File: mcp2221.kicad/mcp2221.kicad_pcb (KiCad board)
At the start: 2 copper layers, 47.2 x 32.8 mm, 26 parts, among them J1 Jumper 32 or 21, J2 Conn_01x04_Male, J3 Conn_01x03_Male, J4 Conn_01x06_Male, J5 Conn_01x03_Male, J6 Conn_01x06_Male, J7 Conn_01x02_Male, J8 Conn_01x02_Male, SW1 SW_Push, SW2 SW_Push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

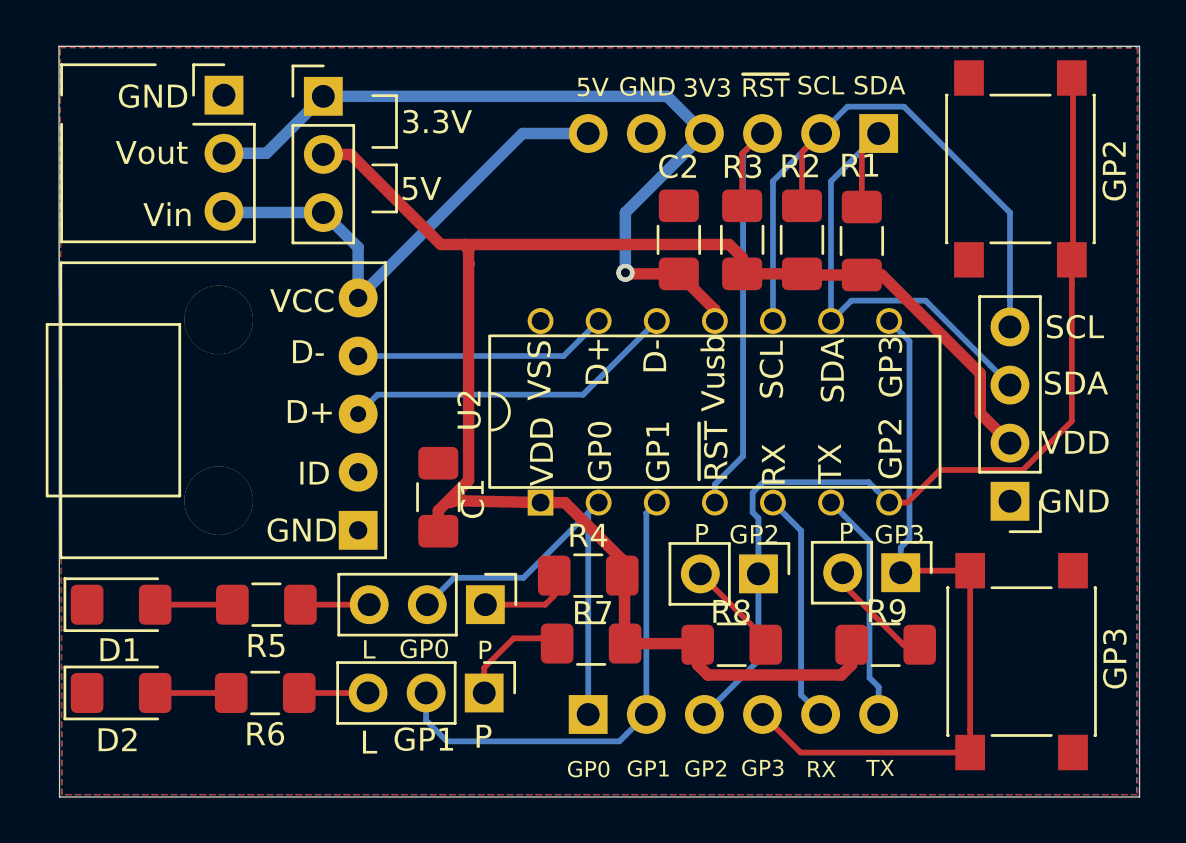
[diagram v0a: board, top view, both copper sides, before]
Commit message: changed to larger pads on SMD-footprints
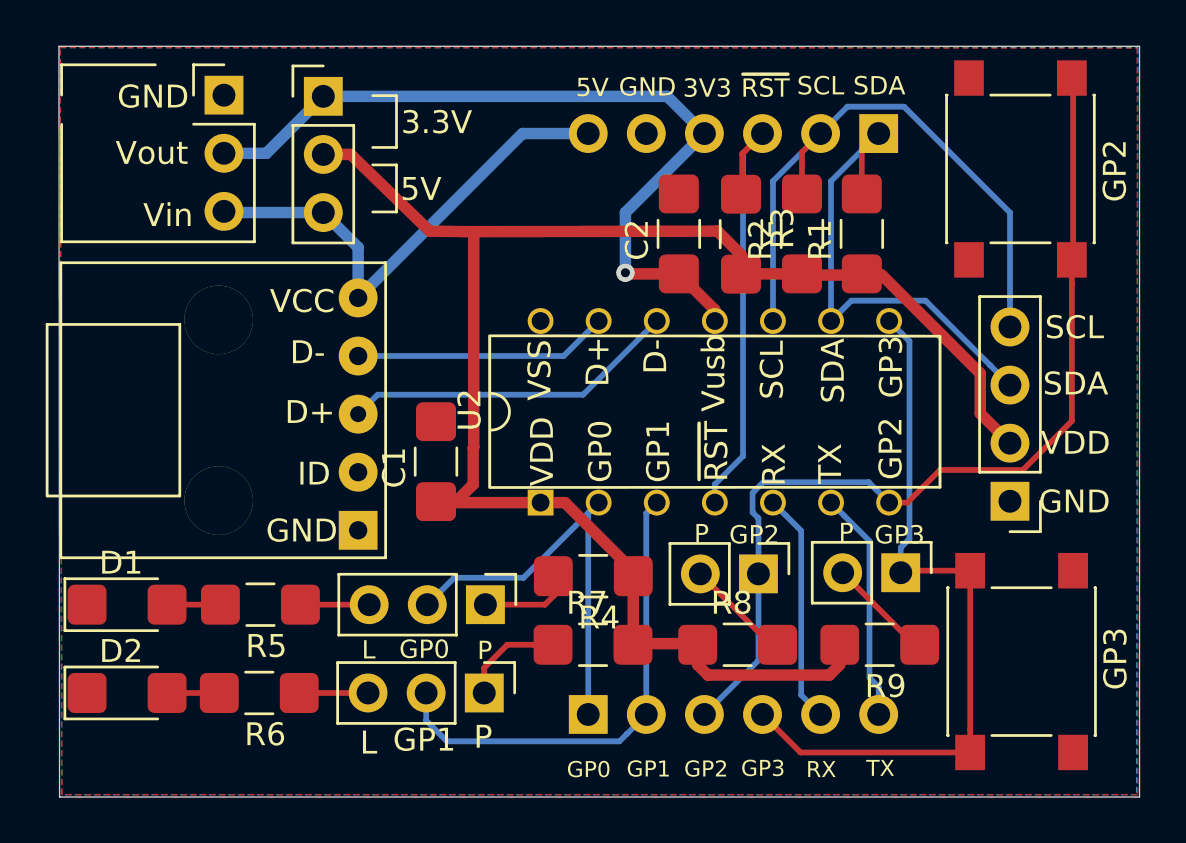
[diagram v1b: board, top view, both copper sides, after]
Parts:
- C1, C2: footprint Capacitor_SMD:C_1206_3216Metric_Pad1.42x1.75mm_HandSolder -> user:C_1206_3216_Pad1.7x1.75mm_BB
- D1, D2: footprint LED_SMD:LED_1206_3216Metric_Pad1.42x1.75mm_HandSolder -> user:LED_1206_3216_Pad1.7x1.75mm_BB
- R1, R2, R3, R4, R5, R6, R7, R8, R9: footprint Resistor_SMD:R_1206_3216Metric_Pad1.42x1.75mm_HandSolder -> user:R_1206_3216_Pad1.7x1.75mm_BB
- moved C1 1.30 mm to (80.8, 67.3)
- moved R3 0.51 mm to (94.1, 56.8)
- moved R4 0.48 mm to (87.9, 72.0)
- moved R7 0.18 mm to (87.4, 75.0)
- moved R1 0.05 mm to (99.4, 57.3)
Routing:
- net Net-(J3-Pad1): track 4.05 -> 4.87 mm

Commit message: changed I2C-connector
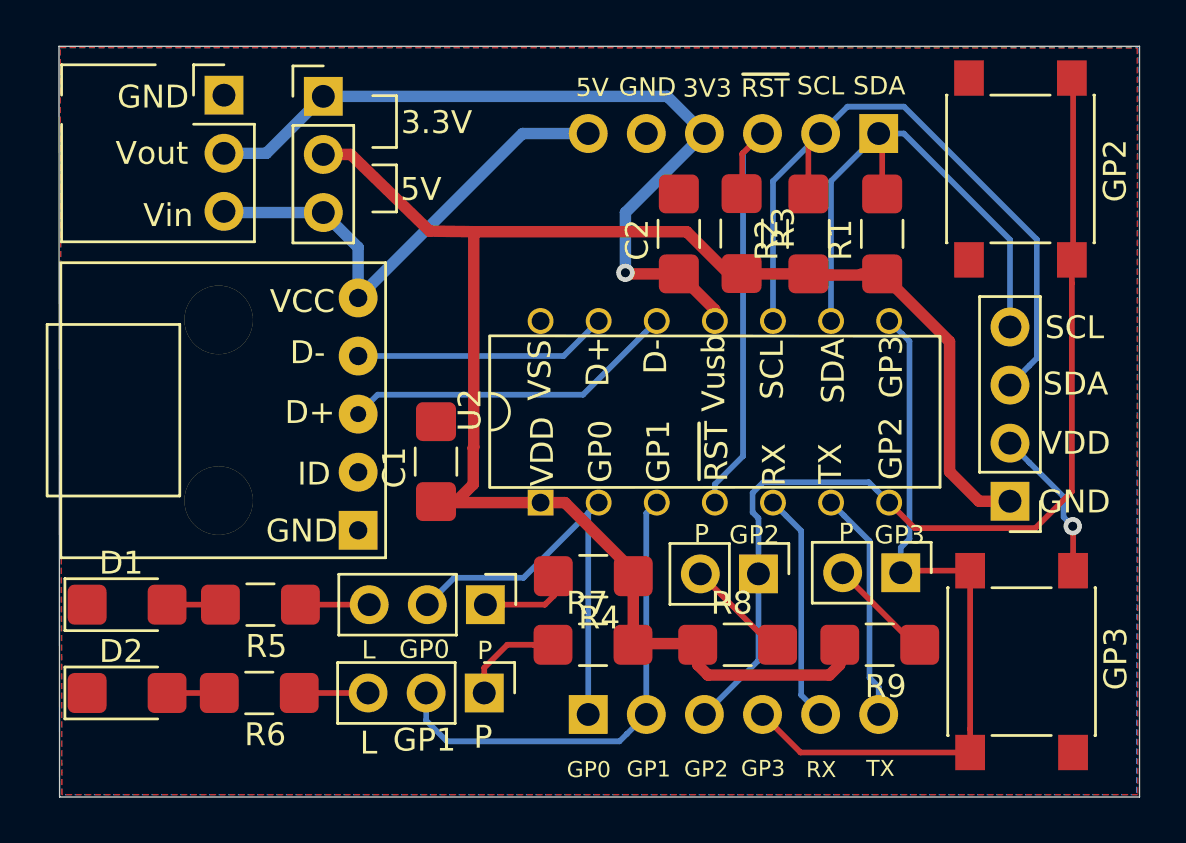
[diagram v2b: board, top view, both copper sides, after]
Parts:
- moved R1 3.51 mm to (100.3, 57.3)
- moved R2 2.34 mm to (97.1, 57.3)
- renumbered R2 to R1, R1 to R2
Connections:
- J2 pad 1: GND -> /VDD
- J2 pad 2: /VDD -> GND
- J2 pad 3: /SDA -> /SCL
- J2 pad 4: /SCL -> /SDA
- R1 pad 2: /SCL -> /SDA
- R2 pad 2: /SDA -> /SCL
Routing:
- net GND: track 0.00 -> 6.72 mm, vias 0 -> 1
- net /VDD: track 74.9 -> 77.8 mm
- net /SCL: track 28.2 -> 31.1 mm
- net /GP2: track 41.8 -> 44.5 mm
- net /SDA: track 22.3 -> 24.3 mm

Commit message: changed revision-number to 8
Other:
- board text added: "Rev 8"
- board text removed: "Rev 7"
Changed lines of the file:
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@@
     (effects (font (size 0.8 0.8) (thickness 0.15)))
   )
-  (gr_text "Rev 7" (at 67.7926 80.2894) (layer B.SilkS)
+  (gr_text "Rev 8" (at 67.7926 80.2894) (layer B.SilkS)
     (effects (font (size 1 1) (thickness 0.15)) (justify mirror))
   )

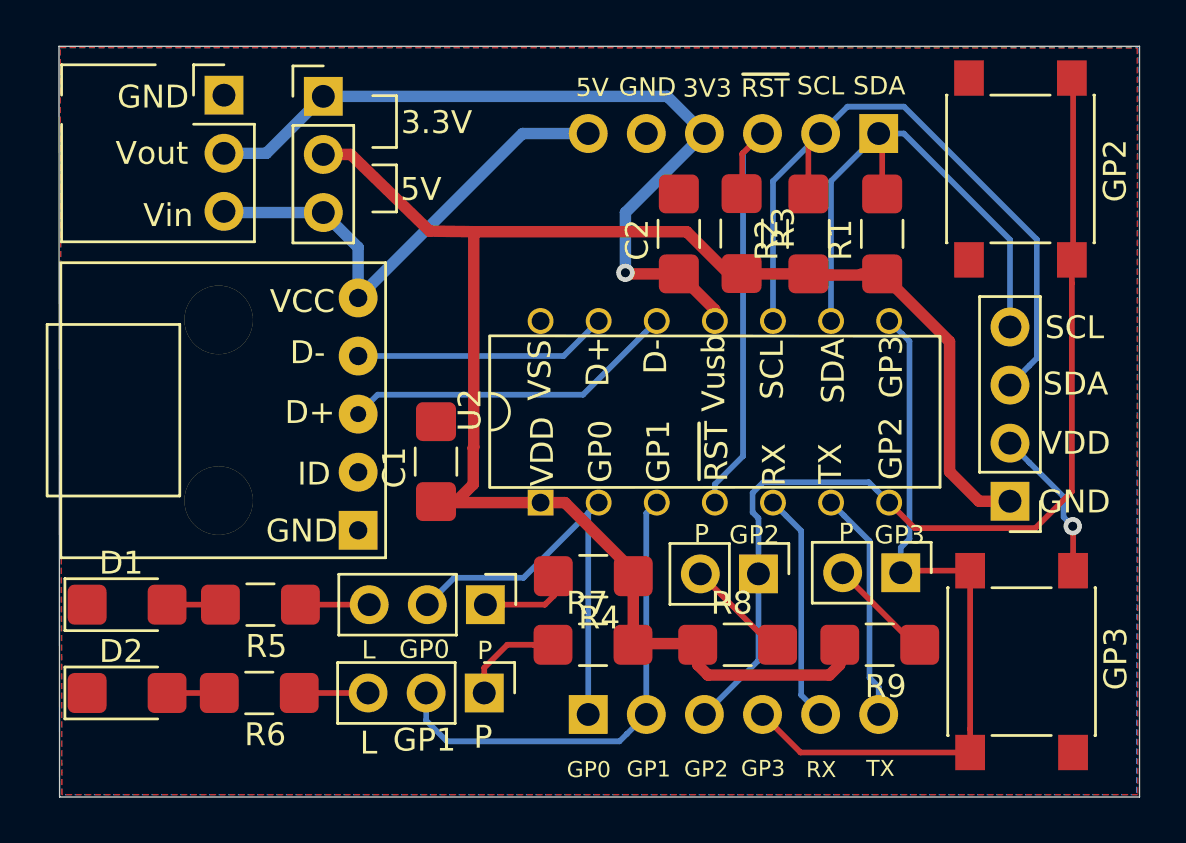
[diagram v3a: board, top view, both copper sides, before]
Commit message: optimzed labels
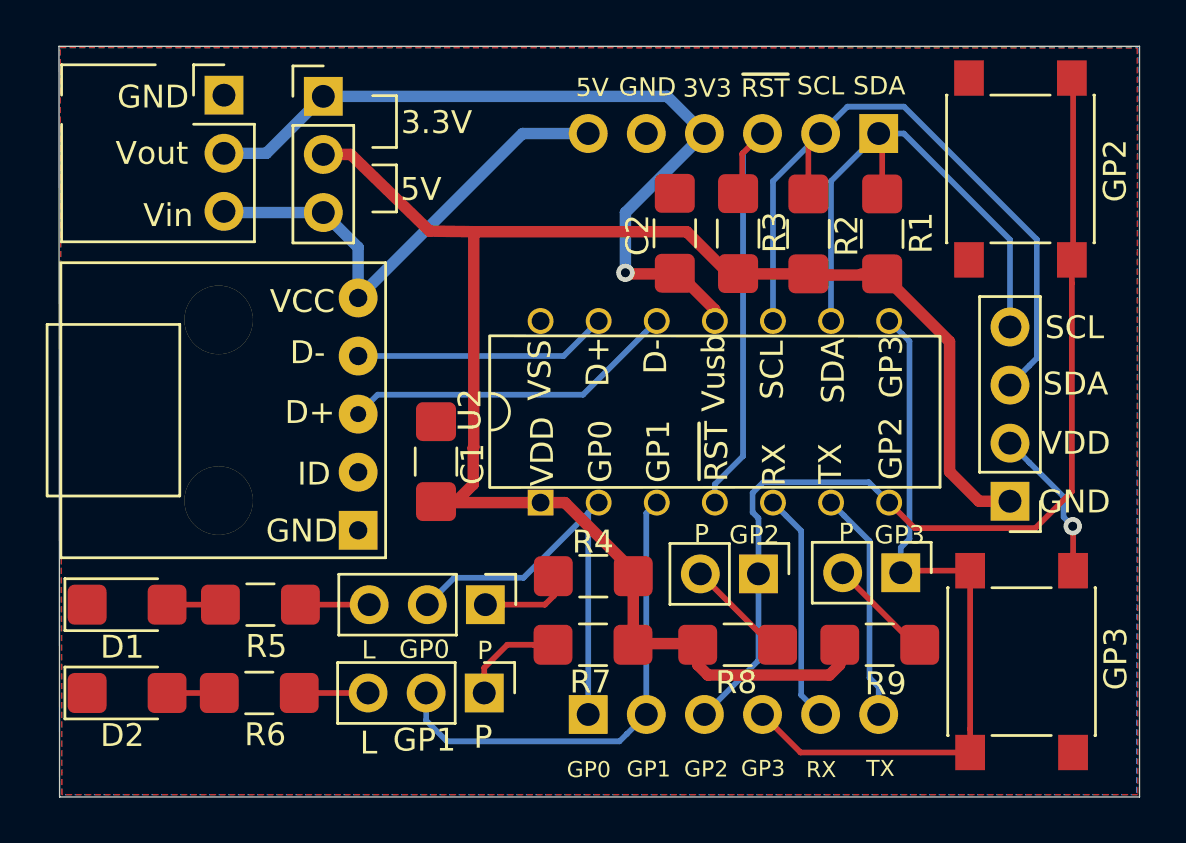
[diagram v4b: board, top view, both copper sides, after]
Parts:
- moved C2 0.18 mm to (91.2, 57.3)
- moved R3 0.15 mm to (94.0, 56.8)
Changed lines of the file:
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@@
     (tags "capacitor handsolder")
     (attr smd)
-    (fp_text reference C1 (at 0 -1.82 90) (layer F.SilkS)
+    (fp_text reference C1 (at 0.1524 1.6002 90) (layer F.SilkS)
       (effects (font (size 1 1) (thickness 0.15)))
     )
@@
   )
   (module user:C_1206_3216_Pad1.7x1.75mm_BB (layer F.Cu)
-    (at 91.3892 57.3278 90)
+    (at 91.2114 57.3024 90)
     (descr "Capacitor SMD 1206 (3216 Metric), square (rectangular) end terminal, IPC_7351 nominal with elongated pad for handsoldering. (Body size source: http://www.tortai-tech.com/upload/download/2011102023233369053.pdf)")
     (tags "capacitor handsolder")
     (attr smd)
-    (fp_text reference C2 (at 0 -1.82 90) (layer F.SilkS)
+    (fp_text reference C2 (at 0.1778 -1.6256 90) (layer F.SilkS)
       (effects (font (size 1 1) (thickness 0.15)))
     )
@@
     (tags "LED handsolder")
     (attr smd)
-    (fp_text reference D1 (at 0 -1.82) (layer F.SilkS)
+    (fp_text reference D1 (at 0.0508 1.8542) (layer F.SilkS)
       (effects (font (size 1 1) (thickness 0.15)))
     )
@@
     (tags "LED handsolder")
     (attr smd)
-    (fp_text reference D2 (at 0 -1.82) (layer F.SilkS)
+    (fp_text reference D2 (at 0.0508 1.8542) (layer F.SilkS)
       (effects (font (size 1 1) (thickness 0.15)))
     )
@@
     (tags "resistor handsolder")
     (attr smd)
-    (fp_text reference R2 (at 0 -1.82 90) (layer F.SilkS)
+    (fp_text reference R2 (at 0.1778 1.6764 90) (layer F.SilkS)
       (effects (font (size 1 1) (thickness 0.15)))
     )
@@
     (tags "resistor handsolder")
     (attr smd)
-    (fp_text reference R1 (at 0 -1.82 90) (layer F.SilkS)
+    (fp_text reference R1 (at 0.3048 1.7018 90) (layer F.SilkS)
       (effects (font (size 1 1) (thickness 0.15)))
     )
@@
   )
   (module user:R_1206_3216_Pad1.7x1.75mm_BB (layer F.Cu)
-    (at 94.1324 56.7944 270)
-    (descr "Resistor SMD 1206 (3216 Metric), square (rectangular) end terminal, IPC_7351 nominal with elongated pad for handsoldering. (Body size source: http://www.tortai-tech.com/upload/download/2011102023233369053.pdf)")
-    (tags "resistor handsolder")
-    (attr smd)
-    (fp_text reference R3 (at 0 -1.82 90) (layer F.SilkS)
+    (at 93.98 56.7944 270)
+    (descr "Resistor SMD 1206 (3216 Metric), square (rectangular) end terminal, IPC_7351 nominal with elongated pad for handsoldering. (Body size source: http://www.tortai-tech.com/upload/download/2011102023233369053.pdf)")
+    (tags "resistor handsolder")
+    (attr smd)
+    (fp_text reference R3 (at 0.2032 -1.6002 90) (layer F.SilkS)
       (effects (font (size 1 1) (thickness 0.15)))
     )
@@
     (tags "resistor handsolder")
     (attr smd)
-    (fp_text reference R4 (at 0 -1.82) (layer F.SilkS)
+    (fp_text reference R4 (at 0.2794 1.4986) (layer F.SilkS)
       (effects (font (size 1 1) (thickness 0.15)))
     )
@@
     (tags "resistor handsolder")
     (attr smd)
-    (fp_text reference R7 (at 0 -1.82) (layer F.SilkS)
+    (fp_text reference R7 (at 0.1524 1.6256) (layer F.SilkS)
       (effects (font (size 1 1) (thickness 0.15)))
     )
@@
     (tags "resistor handsolder")
     (attr smd)
-    (fp_text reference R8 (at 0 -1.82) (layer F.SilkS)
+    (fp_text reference R8 (at 0.2032 1.651) (layer F.SilkS)
       (effects (font (size 1 1) (thickness 0.15)))
     )
@@
     (tags "resistor handsolder")
     (attr smd)
-    (fp_text reference R9 (at 0 -1.82) (layer F.SilkS)
-      (effects (font (size 1 1) (thickness 0.15)))
-    )
+    (fp_text reference R9 (at 0 -1.7018) (layer F.SilkS)
+      (effects (font (size 1 1) (thickness 0.15)))
+    )

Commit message: added description of GPs on back of pcb
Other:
- board text added: "GP0: IO, LED-RX GP1: IO, LED-TX, ADC1 GP2: IO, DAC, ADC2 GP3: IO, DAC, ADC3"
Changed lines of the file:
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@@
   (general
     (thickness 1.6)
-    (drawings 43)
+    (drawings 44)
     (tracks 158)
     (zones 0)
@@
     )
   )
+  (gr_text "GP0: IO, LED-RX\nGP1: IO, LED-TX, ADC1\nGP2: IO, DAC, ADC2\nGP3: IO, DAC, ADC3" (at 102.5906 64.77) (layer B.SilkS)
+    (effects (font (size 1 1) (thickness 0.15)) (justify left mirror))
+  )
   (gr_text GP2 (at 110.4646 54.3052 90) (layer F.SilkS)

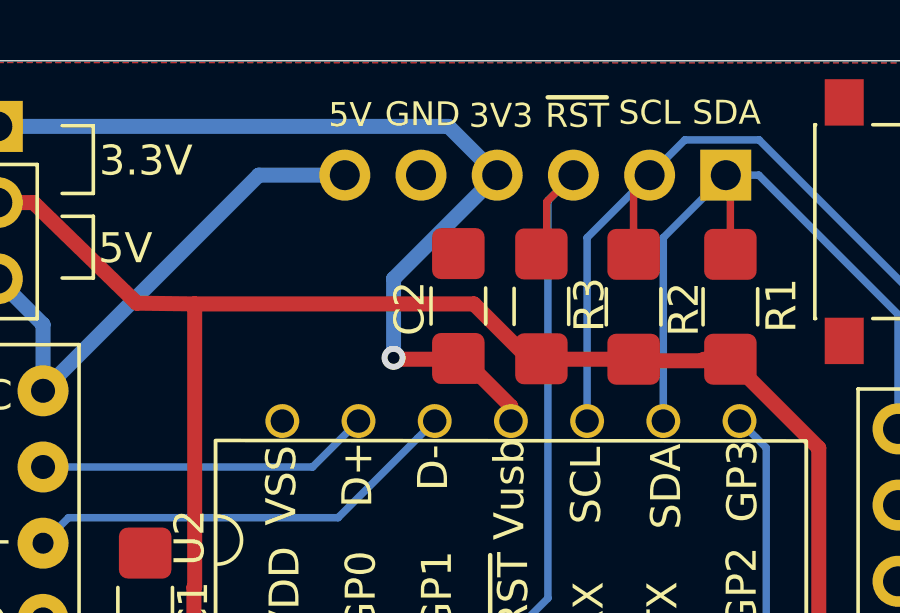
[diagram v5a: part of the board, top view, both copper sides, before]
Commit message: Rev 9: don't connect Vusb to 3.3V / changed R for LEDs to 150
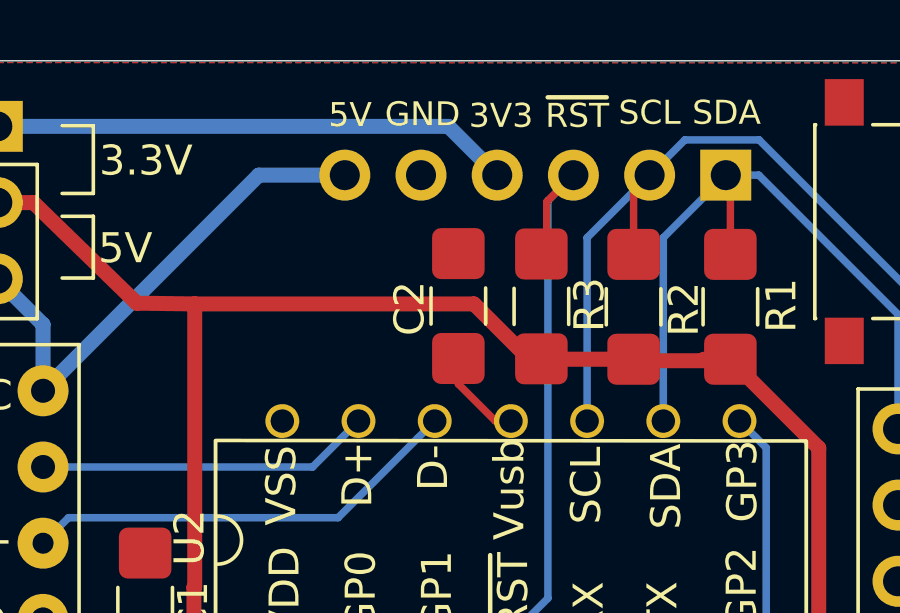
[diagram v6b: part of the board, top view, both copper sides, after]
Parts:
- R5, R6: value 1K -> 150
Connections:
- C2 pad 1: /3.3V -> Net-(C2-Pad1)
- U2 pad 11: /3.3V -> Net-(C2-Pad1)
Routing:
- net /3.3V: track 35.2 -> 22.7 mm, vias 1 -> 0
- net Net-(C2-Pad1): track 0.00 -> 3.11 mm
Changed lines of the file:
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@@
     (thickness 1.6)
     (drawings 44)
-    (tracks 158)
+    (tracks 155)
     (zones 0)
     (modules 26)
-    (nets 25)
+    (nets 26)
   )
   (page A4)
@@
   (net 23 "Net-(J7-Pad2)")
   (net 24 "Net-(J8-Pad2)")
+  (net 25 "Net-(C2-Pad1)")
   (net_class Default "Dies ist die voreingestellte Netzklasse."
     (clearance 0.2)
@@
     (add_net /~RST~)
     (add_net GND)
+    (add_net "Net-(C2-Pad1)")
     (add_net "Net-(D1-Pad2)")
     (add_net "Net-(D2-Pad2)")
@@
       (net 12 /SCL))
     (pad 11 thru_hole circle (at 3.97 0 90) (size 1.13 1.13) (drill 0.78) (layers *.Cu *.Mask)
-      (net 17 /3.3V))
+      (net 25 "Net-(C2-Pad1)"))
     (pad 12 thru_hole circle (at 3.97 -2.54 90) (size 1.13 1.13) (drill 0.78) (layers *.Cu *.Mask)
       (net 15 /USB-D-))
@@
     )
     (pad 1 smd roundrect (at -1.4875 0 90) (size 1.7 1.75) (layers F.Cu F.Paste F.Mask) (roundrect_rratio 0.175)
-      (net 17 /3.3V))
+      (net 25 "Net-(C2-Pad1)"))
     (pad 2 smd roundrect (at 2.0075 0 90) (size 1.7 1.75) (layers F.Cu F.Paste F.Mask) (roundrect_rratio 0.175)
       (net 1 GND))
@@
       (effects (font (size 1 1) (thickness 0.15)))
     )
-    (fp_text value 1K (at 0 1.82) (layer F.Fab)
+    (fp_text value 150 (at 0 1.82) (layer F.Fab)
       (effects (font (size 1 1) (thickness 0.15)))
     )
@@
       (effects (font (size 1 1) (thickness 0.15)))
     )
-    (fp_text value 1K (at 0 1.82) (layer F.Fab)
+    (fp_text value 150 (at 0 1.82) (layer F.Fab)
       (effects (font (size 1 1) (thickness 0.15)))
     )
@@
   (segment (start 78.218399 64.097801) (end 87.202399 64.097801) (width 0.25) (layer B.Cu) (net 15))
   (segment (start 77.3684 64.9478) (end 78.218399 64.097801) (width 0.25) (layer B.Cu) (net 15))
-  (via (at 89.0524 58.768) (size 0.8) (drill 0.4) (layers F.Cu B.Cu) (net 17))
-  (segment (start 91.3892 58.8153) (end 89.0997 58.8153) (width 0.5) (layer F.Cu) (net 17))
-  (segment (start 92.964 60.3901) (end 91.3892 58.8153) (width 0.5) (layer F.Cu) (net 17))
-  (segment (start 92.964 60.8762) (end 92.964 60.3901) (width 0.5) (layer F.Cu) (net 17))
   (segment (start 73.3552 53.5432) (end 75.8444 51.054) (width 0.5) (layer B.Cu) (net 17))
   (segment (start 71.501 53.5432) (end 73.3552 53.5432) (width 0.5) (layer B.Cu) (net 17))
   (segment (start 90.8812 51.054) (end 92.5068 52.6796) (width 0.5) (layer B.Cu) (net 17))
   (segment (start 75.8444 51.054) (end 90.8812 51.054) (width 0.5) (layer B.Cu) (net 17))
-  (segment (start 89.0524 56.134) (end 92.5068 52.6796) (width 0.5) (layer B.Cu) (net 17))
-  (segment (start 89.0524 58.768) (end 89.0524 56.134) (width 0.5) (layer B.Cu) (net 17))
   (segment (start 77.3684 57.658) (end 75.8444 56.134) (width 0.5) (layer B.Cu) (net 18))
   (segment (start 77.3684 59.8678) (end 77.3684 57.658) (width 0.5) (layer B.Cu) (net 18))
@@
   (segment (start 101.7016 75.0316) (end 101.9191 75.0316) (width 0.25) (layer F.Cu) (net 24))
   (segment (start 98.552 71.882) (end 101.7016 75.0316) (width 0.25) (layer F.Cu) (net 24))
+  (segment (start 92.4477 60.8762) (end 92.964 60.8762) (width 0.25) (layer F.Cu) (net 25))
+  (segment (start 91.2114 59.6399) (end 92.4477 60.8762) (width 0.25) (layer F.Cu) (net 25))
+  (segment (start 91.2114 58.7899) (end 91.2114 59.6399) (width 0.25) (layer F.Cu) (net 25))
   (zone (net 1) (net_name GND) (layer F.Cu) (hatch edge 0.508)
     (connect_pads (clearance 0.508))
